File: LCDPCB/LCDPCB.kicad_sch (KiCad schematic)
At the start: 32 parts, among them J1 Sockets, J2 Hot Plug, J3 Programming Header, J4 Conn_01x08_Male, J5 Conn_01x08_Male, SW1 SW_Push, U1 STM32F091RCT6, U2 LD1117S12TR_SOT223

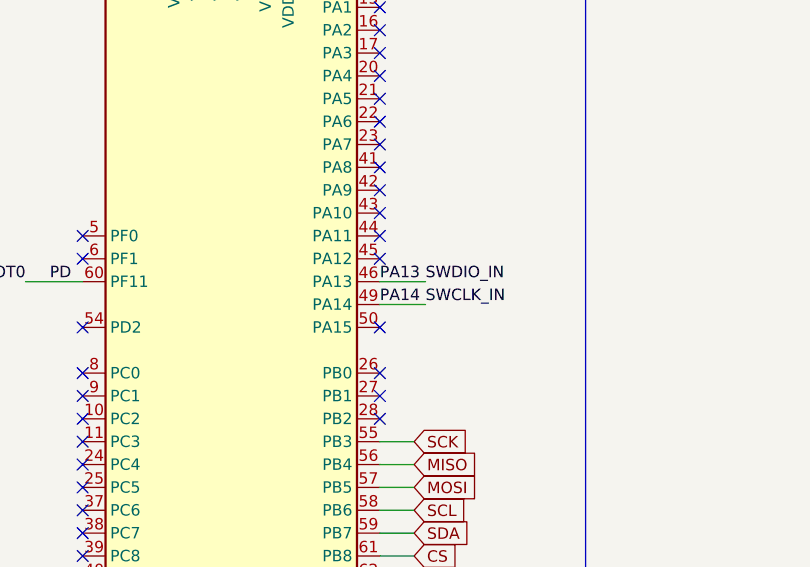
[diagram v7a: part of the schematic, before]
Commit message: renamed pa13 and 14
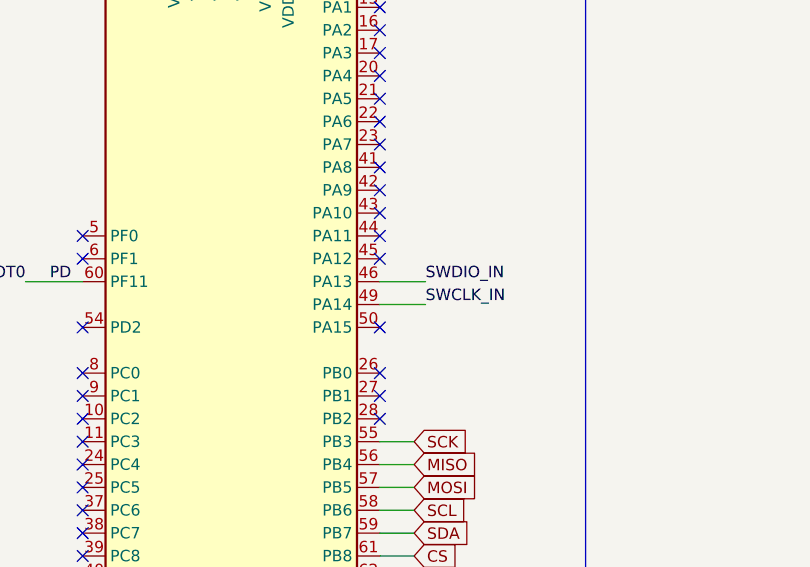
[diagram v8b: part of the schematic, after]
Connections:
- net PA13: no longer J3.2 (Pin_2), U1.46 (PA13)
- net PA14: no longer J3.6 (Pin_6), U1.49 (PA14)
- new net SWCLK_IN: J3.6 (Pin_6), U1.49 (PA14)
- new net SWDIO_IN: J3.2 (Pin_2), U1.46 (PA13)
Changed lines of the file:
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@@
     (effects (font (size 1.27 1.27)) (justify right bottom))
-  )
-  (label "PA14" (at 167.64 96.52 0)
-    (effects (font (size 1.27 1.27)) (justify left bottom))
-  )
-  (label "PA13" (at 167.64 93.98 0)
-    (effects (font (size 1.27 1.27)) (justify left bottom))
   )
   (label "BOOT0" (at 245.11 62.23 0)
